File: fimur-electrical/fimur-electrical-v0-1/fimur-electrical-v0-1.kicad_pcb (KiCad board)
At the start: 2 copper layers, 37 x 25 mm, 18 parts, among them J1 Conn_01x04_Pin, J2 Conn_01x04_Pin, J3 Conn_02x03_Odd_Even, U1 NCP163AFCS180T2G, U2 ICM-20948, U3 ICM-20948

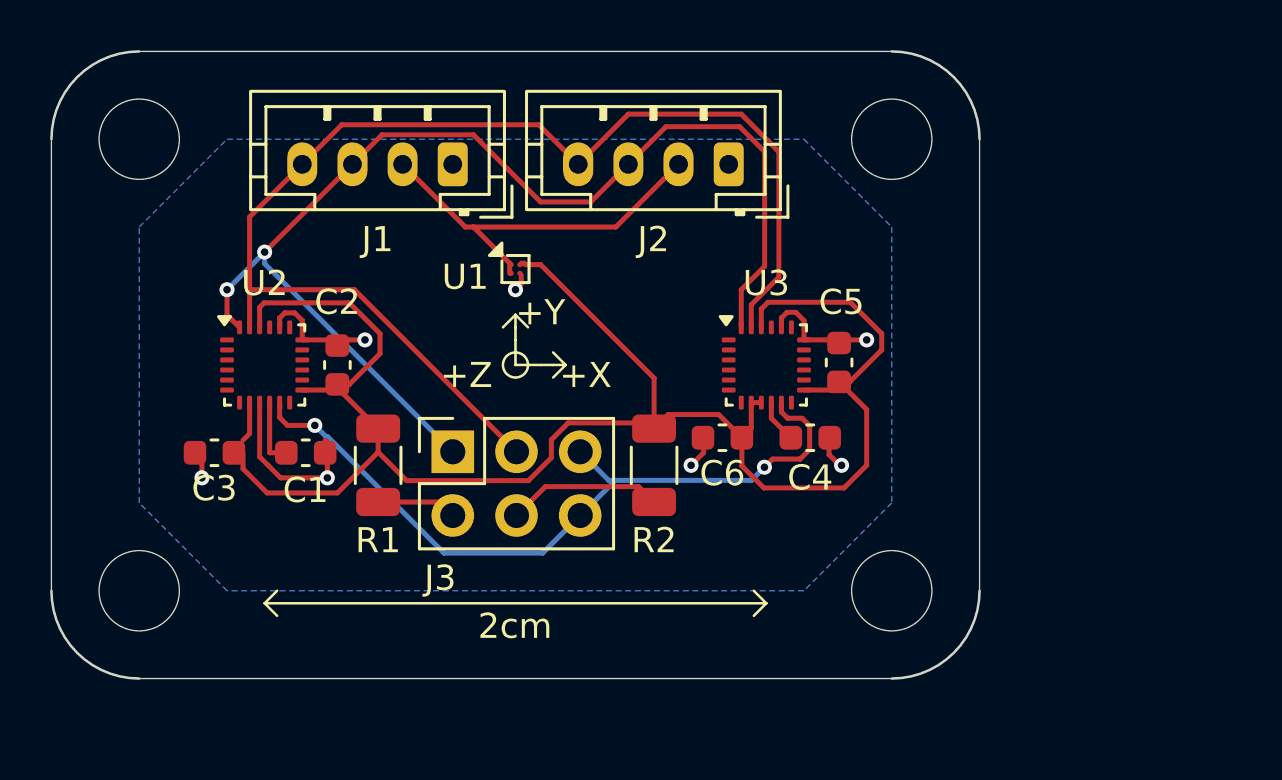
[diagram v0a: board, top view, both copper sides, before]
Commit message: multiplex schematic and layout and standardization with 2-imu board
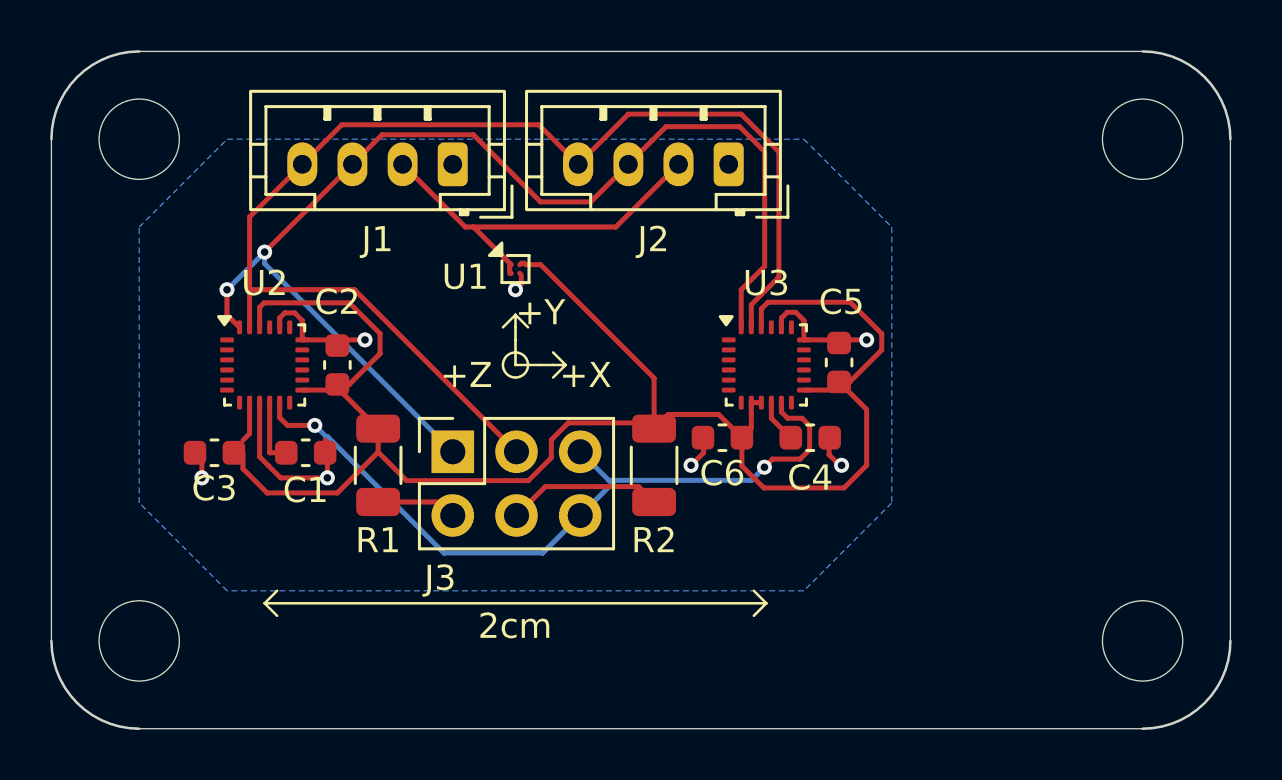
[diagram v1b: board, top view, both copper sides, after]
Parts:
- moved REF** 10.2 mm to (125.0, 111.0)
- moved REF** 10.0 mm to (125.0, 91.0)
- moved REF** 2.00 mm to (85.0, 111.0)
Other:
- board size 37 x 25 mm -> 47 x 27 mm
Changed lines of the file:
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@@
 	(footprint "MountingHole:MountingHole_3.2mm_M3"
 		(layer "F.Cu")
-		(at 115 91)
+		(at 125 91)
 		(descr "Mounting Hole 3.2mm, M3, no annular, generated by kicad-footprint-generator mountinghole.py")
 		(tags "mountinghole M3")
@@
 	(footprint "MountingHole:MountingHole_3.2mm_M3"
 		(layer "F.Cu")
-		(at 115 109)
+		(at 125 111)
 		(descr "Mounting Hole 3.2mm, M3, no annular, generated by kicad-footprint-generator mountinghole.py")
 		(tags "mountinghole M3")
@@
 	(footprint "MountingHole:MountingHole_3.2mm_M3"
 		(layer "F.Cu")
-		(at 85 109)
+		(at 85 111)
 		(descr "Mounting Hole 3.2mm, M3, no annular, generated by kicad-footprint-generator mountinghole.py")
 		(tags "mountinghole M3")
@@
 	(gr_rect
 		(start 85 91)
-		(end 115 109)
+		(end 125 111)
 		(stroke
 			(width 0.1)
@@
 	)
 	(gr_line
-		(start 118.5 91)
-		(end 118.5 109)
+		(start 128.5 91)
+		(end 128.5 111)
 		(stroke
 			(width 0.05)
@@
 	)
 	(gr_arc
-		(start 115 87.5)
-		(mid 117.474874 88.525126)
-		(end 118.5 91)
+		(start 125 87.5)
+		(mid 127.474874 88.525126)
+		(end 128.5 91)
 		(stroke
 			(width 0.1)
@@
 	)
 	(gr_line
-		(start 115 112.5)
-		(end 85 112.5)
+		(start 125 114.5)
+		(end 85 114.5)
 		(stroke
 			(width 0.05)
@@
 	)
 	(gr_arc
-		(start 85 112.5)
-		(mid 82.525126 111.474874)
-		(end 81.5 109)
+		(start 85 114.5)
+		(mid 82.525126 113.474874)
+		(end 81.5 111)
 		(stroke
 			(width 0.1)
@@
 	)
 	(gr_line
-		(start 81.5 109)
+		(start 81.5 111)
 		(end 81.5 91)
 		(stroke
@@
 	)
 	(gr_arc
-		(start 118.5 109)
-		(mid 117.474874 111.474874)
-		(end 115 112.5)
+		(start 128.5 111)
+		(mid 127.474874 113.474874)
+		(end 125 114.5)
 		(stroke
 			(width 0.1)
@@
 	(gr_line
 		(start 85 87.5)
-		(end 115 87.5)
+		(end 125 87.5)
 		(stroke
 			(width 0.05)
